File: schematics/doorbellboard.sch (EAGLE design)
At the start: 6 parts

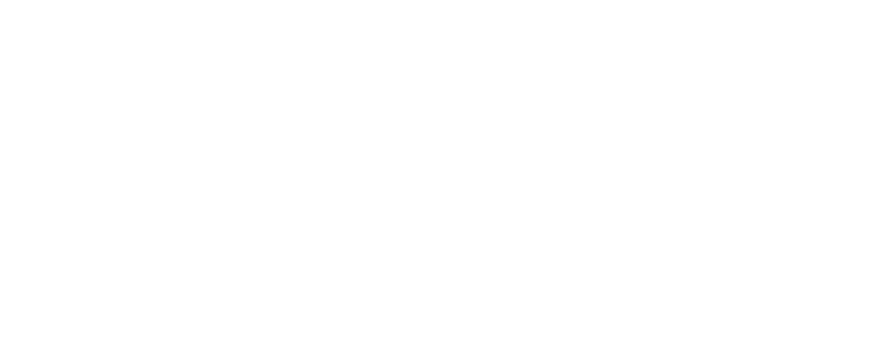
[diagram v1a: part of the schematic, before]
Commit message: Add name/website/version
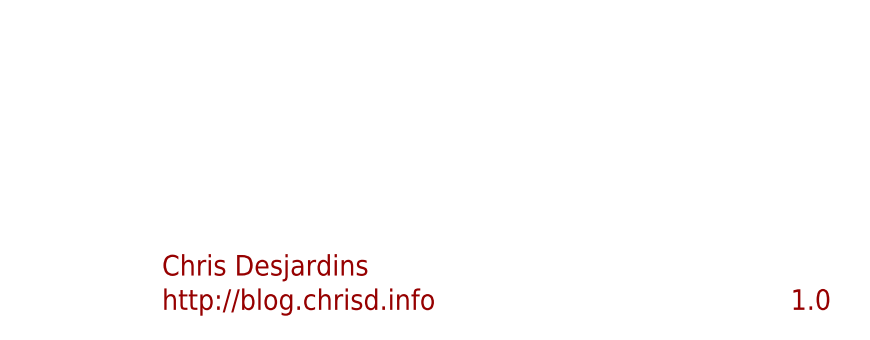
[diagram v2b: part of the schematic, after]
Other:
- note added: "1.0"
- note added: "Chris Desjardins"
- note added: "http://blog.chrisd.info"
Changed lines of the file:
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@@
 <sheet>
 <plain>
+<text x="167.64" y="11.43" size="2.286" layer="94">Chris Desjardins</text>
+<text x="237.49" y="7.62" size="2.286" layer="94">1.0</text>
+<text x="167.64" y="7.62" size="2.286" layer="94">http://blog.chrisd.info</text>
 </plain>
 <instances>

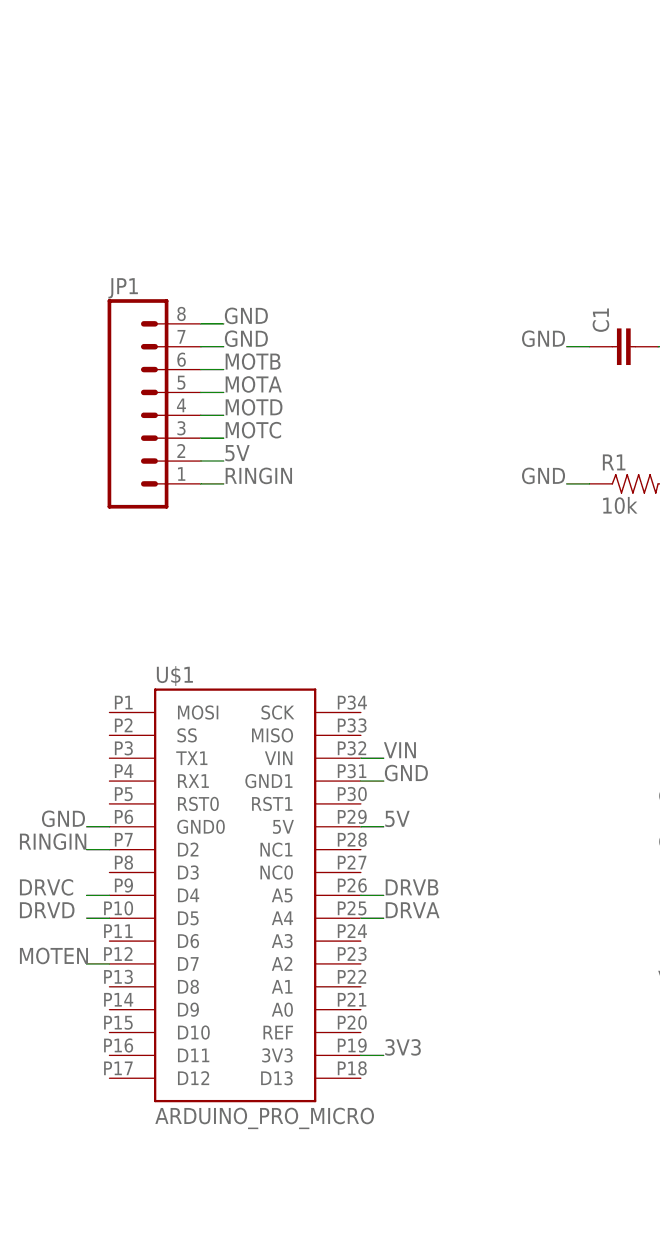
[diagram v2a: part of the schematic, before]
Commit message: Add some LEDs
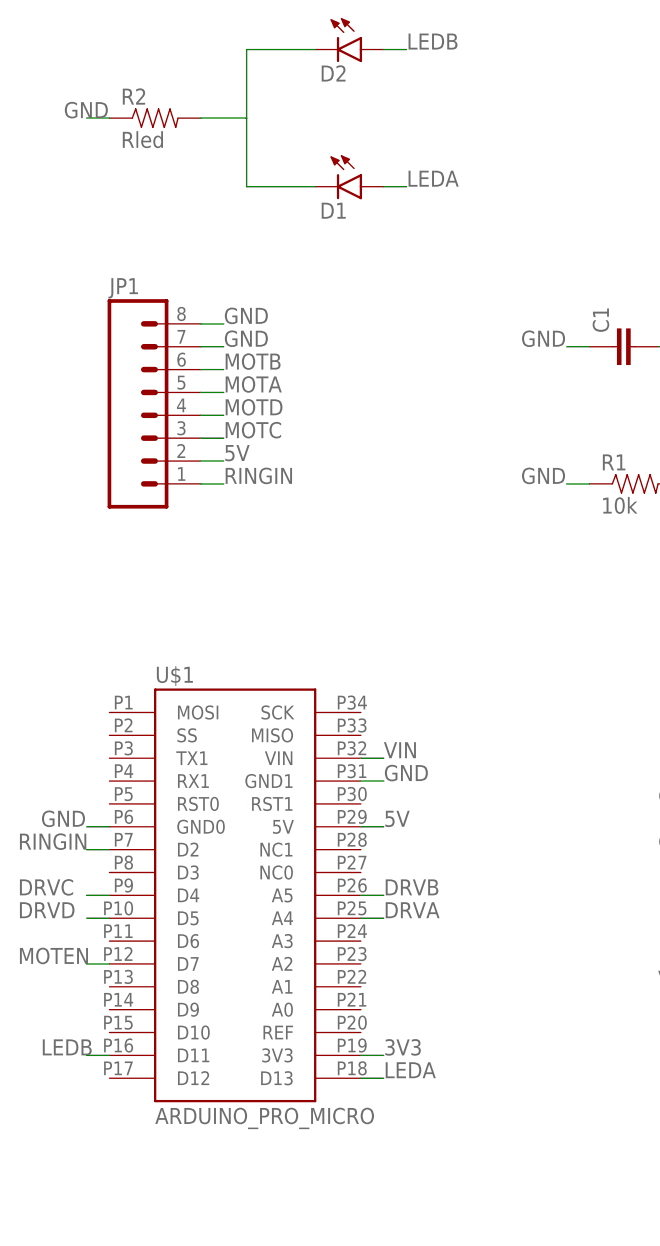
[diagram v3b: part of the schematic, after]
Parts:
- added D1, D2: (no value), SparkFun-LED:LED-3MM-NO_SILK
- added R2: Rled, SparkFun-Resistors:10KOHM-1/4W-1%(PTH)HORIZ
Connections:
- new net LEDA: D1.A, U$1.D13
- new net LEDB: D2.A, U$1.D11
- new net LEDOUT: D1.C, D2.C, R2.2
- net GND: now also R2.1
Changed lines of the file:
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@@
 <part name="U$2" library="desjardins" deviceset="SN754410" device=""/>
 <part name="JP2" library="SparkFun-Connectors" deviceset="POWER_JACK" device="PTH"/>
+<part name="D1" library="SparkFun-LED" deviceset="LED" device="-3MM-NO_SILK"/>
+<part name="D2" library="SparkFun-LED" deviceset="LED" device="-3MM-NO_SILK"/>
+<part name="R2" library="SparkFun-Resistors" deviceset="10KOHM-1/4W-1%(PTH)" device="HORIZ" value="Rled"/>
 </parts>
 <sheets>
@@
 <instance part="U$2" gate="G$1" x="114.3" y="45.72"/>
 <instance part="JP2" gate="G$1" x="134.62" y="96.52"/>
+<instance part="D1" gate="G$1" x="58.42" y="121.92" rot="R270"/>
+<instance part="D2" gate="G$1" x="58.42" y="137.16" rot="R270"/>
+<instance part="R2" gate="G$1" x="35.56" y="129.54"/>
 </instances>
 <busses>
@@
 <label x="76.2" y="88.9" size="1.778" layer="95"/>
 </segment>
+<segment>
+<pinref part="R2" gate="G$1" pin="1"/>
+<wire x1="30.48" y1="129.54" x2="27.94" y2="129.54" width="0.1524" layer="91"/>
+<label x="25.4" y="129.54" size="1.778" layer="95"/>
+</segment>
 </net>
 <net name="MOTA" class="0">
@@
 </segment>
 </net>
+<net name="LEDA" class="0">
+<segment>
+<pinref part="U$1" gate="G$1" pin="D13"/>
+<wire x1="58.42" y1="22.86" x2="60.96" y2="22.86" width="0.1524" layer="91"/>
+<label x="60.96" y="22.86" size="1.778" layer="95"/>
+</segment>
+<segment>
+<pinref part="D1" gate="G$1" pin="A"/>
+<wire x1="60.96" y1="121.92" x2="63.5" y2="121.92" width="0.1524" layer="91"/>
+<label x="63.5" y="121.92" size="1.778" layer="95"/>
+</segment>
+</net>
+<net name="LEDB" class="0">
+<segment>
+<pinref part="U$1" gate="G$1" pin="D11"/>
+<wire x1="30.48" y1="25.4" x2="27.94" y2="25.4" width="0.1524" layer="91"/>
+<label x="22.86" y="25.4" size="1.778" layer="95"/>
+</segment>
+<segment>
+<pinref part="D2" gate="G$1" pin="A"/>
+<wire x1="60.96" y1="137.16" x2="63.5" y2="137.16" width="0.1524" layer="91"/>
+<label x="63.5" y="137.16" size="1.778" layer="95"/>
+</segment>
+</net>
+<net name="LEDOUT" class="0">
+<segment>
+<pinref part="D2" gate="G$1" pin="C"/>
+<pinref part="D1" gate="G$1" pin="C"/>
+<wire x1="53.34" y1="121.92" x2="45.72" y2="121.92" width="0.1524" layer="91"/>
+<wire x1="45.72" y1="121.92" x2="45.72" y2="129.54" width="0.1524" layer="91"/>
+<pinref part="R2" gate="G$1" pin="2"/>
+<wire x1="45.72" y1="129.54" x2="40.64" y2="129.54" width="0.1524" layer="91"/>
+<wire x1="53.34" y1="137.16" x2="45.72" y2="137.16" width="0.1524" layer="91"/>
+<wire x1="45.72" y1="137.16" x2="45.72" y2="129.54" width="0.1524" layer="91"/>
+</segment>
+</net>
